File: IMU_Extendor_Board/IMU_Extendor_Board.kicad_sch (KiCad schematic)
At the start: 72 parts, among them J101 USB_C_Receptacle_USB2.0_16P, J102 Conn_01x02_Pin, J201 DNP, J501 Conn_01x06_Pin, J601 Conn_01x07_Pin, J702 Conn_01x10_Pin, J703 Conn_01x04_Pin, U101 XC6210B332PR-G, U102 USBLC6-2SC6, U201 STM32F722RETx, U401 BNO086, U501 ICM-42688-P, Y202 Crystal, Y203 ECS-327KE, Y401 ECS-327KE, Y501 ECS-327KE

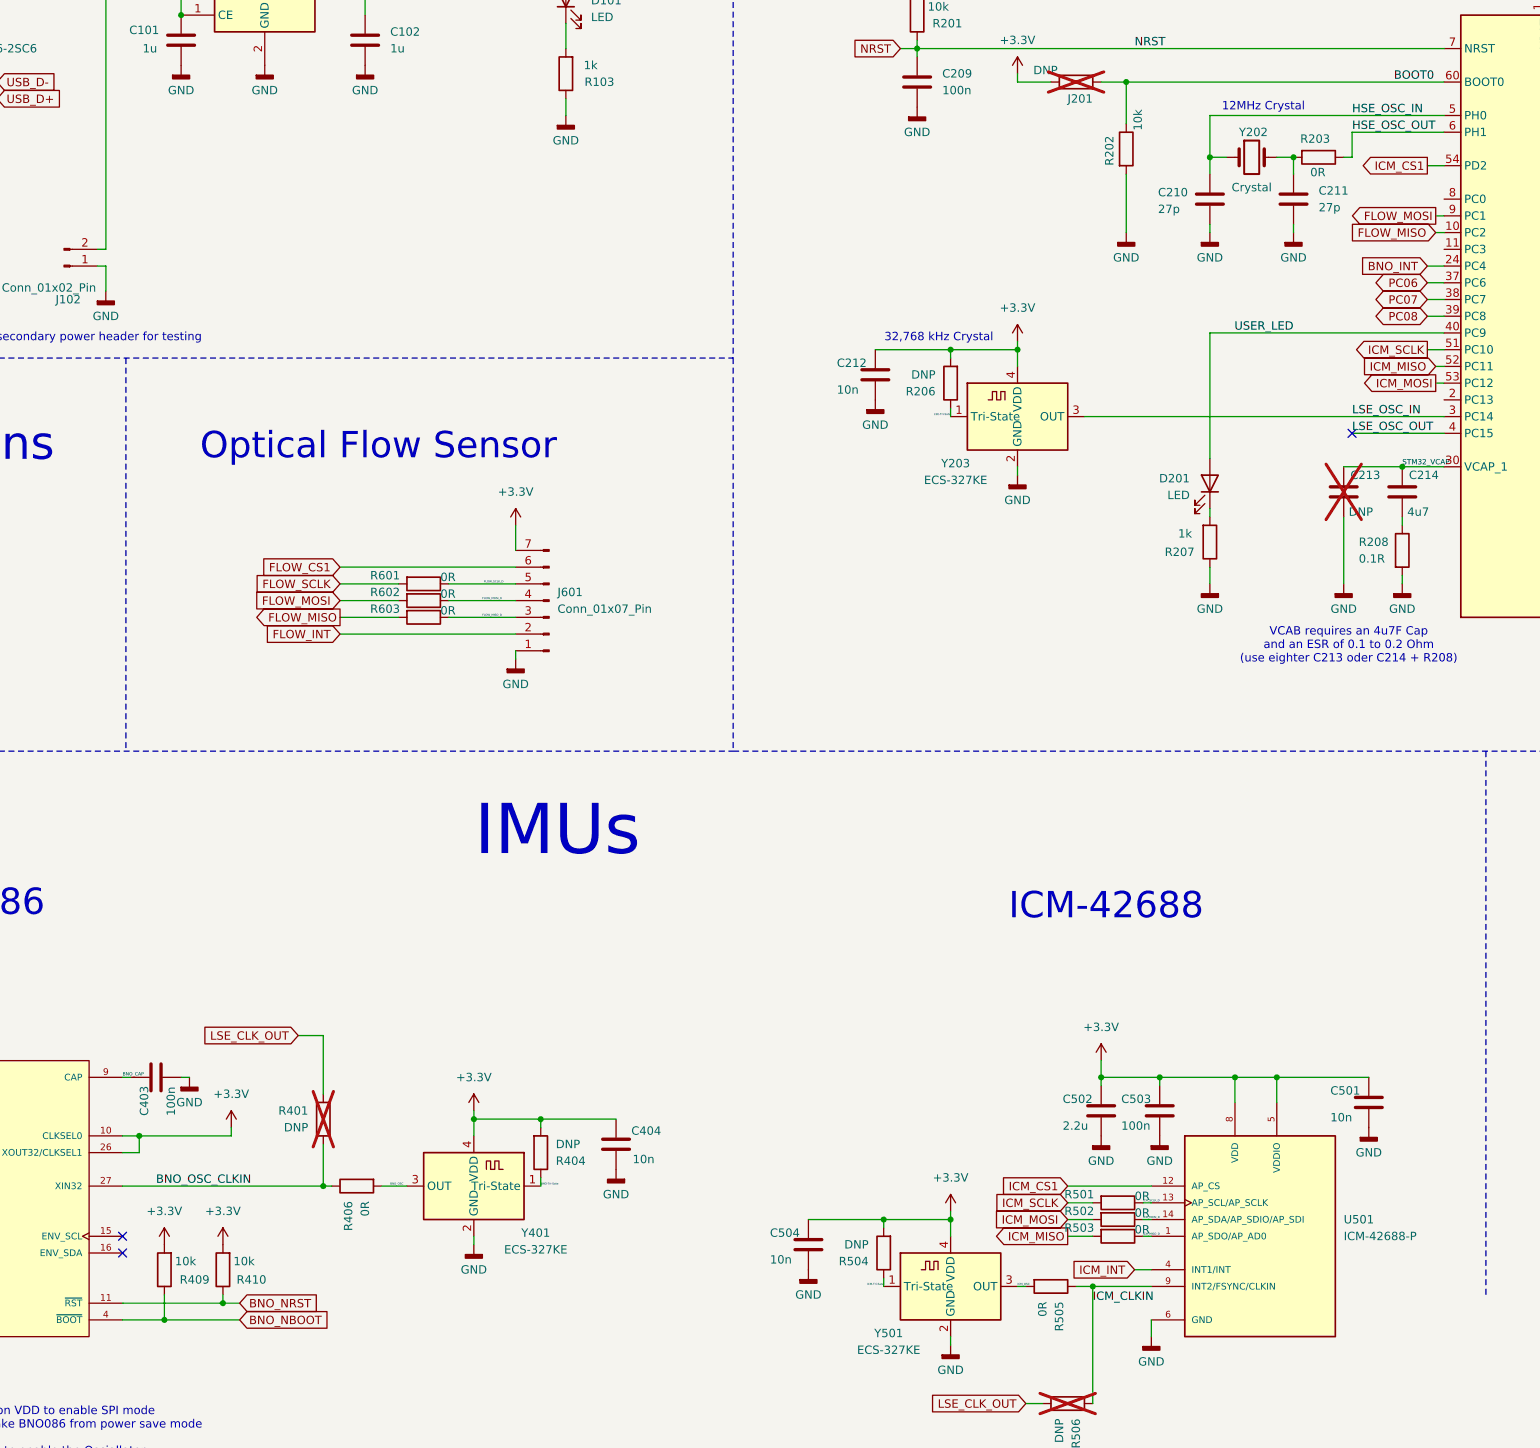
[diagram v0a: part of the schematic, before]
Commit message: modifide the schematic to fix oscillator GND and in pcb; added ENV I2C pullpus in shematic
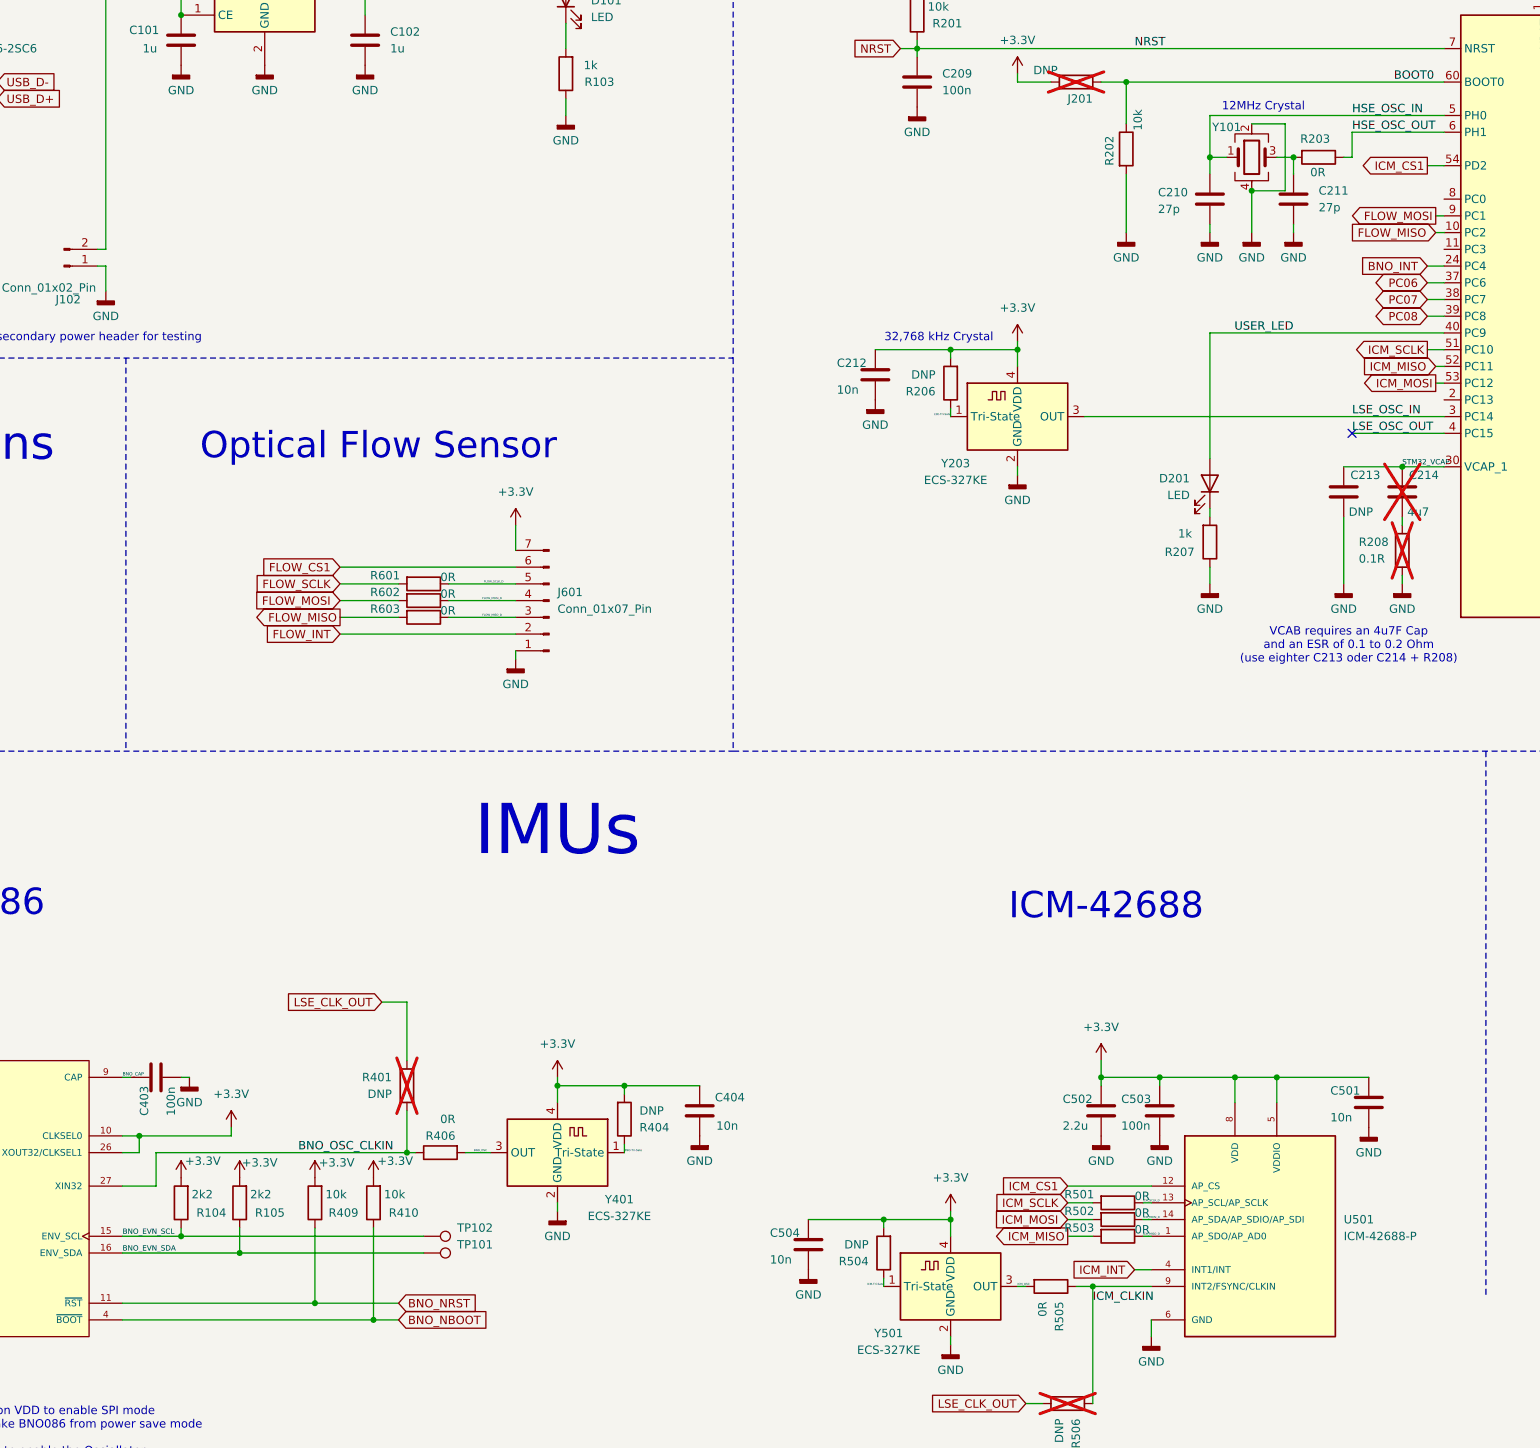
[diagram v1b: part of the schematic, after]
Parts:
- removed Y202: Crystal, Crystal:Crystal_SMD_Abracon_ABM8G-4Pin_3.2x2.5mm, symbol Device:Crystal
- added R104, R105: 2k2, MYFootprints:0402_1005Metric_Pad0.74x0.62mm_HandSolder, symbol Device:R
- added TP101, TP102: TestPoint, TestPoint:TestPoint_Pad_1.0x1.0mm, symbol Connector:TestPoint
- added Y101: Crystal_GND24, Crystal:Crystal_SMD_Abracon_ABM8G-4Pin_3.2x2.5mm, symbol Device:Crystal_GND24
- C213: now fitted
- C214, R208: now not fitted
- renumbered R410 to R409, R409 to R410
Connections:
- net +3.3V: now also R104.2, R105.2
- net GND: now also Y101.2, Y101.4
- net HSE_OSC_IN: now also Y101.1
- net at C211.1, R203.2: now also Y101.3
- net BNO_EVN_SCL: now reaches U401.15 (ENV_SCL)
- net BNO_EVN_SCL: now also R104.1, TP102.1
- net BNO_EVN_SDA: now reaches U401.16 (ENV_SDA)
- net BNO_EVN_SDA: now also R105.1, TP101.1
- no-connect marks 5 -> 3
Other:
- moved on the sheet: C404, R401, R404, R406, R409, R410, Y401
